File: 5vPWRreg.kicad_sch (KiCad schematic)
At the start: 25 parts, among them U9 TPS54561DPRR

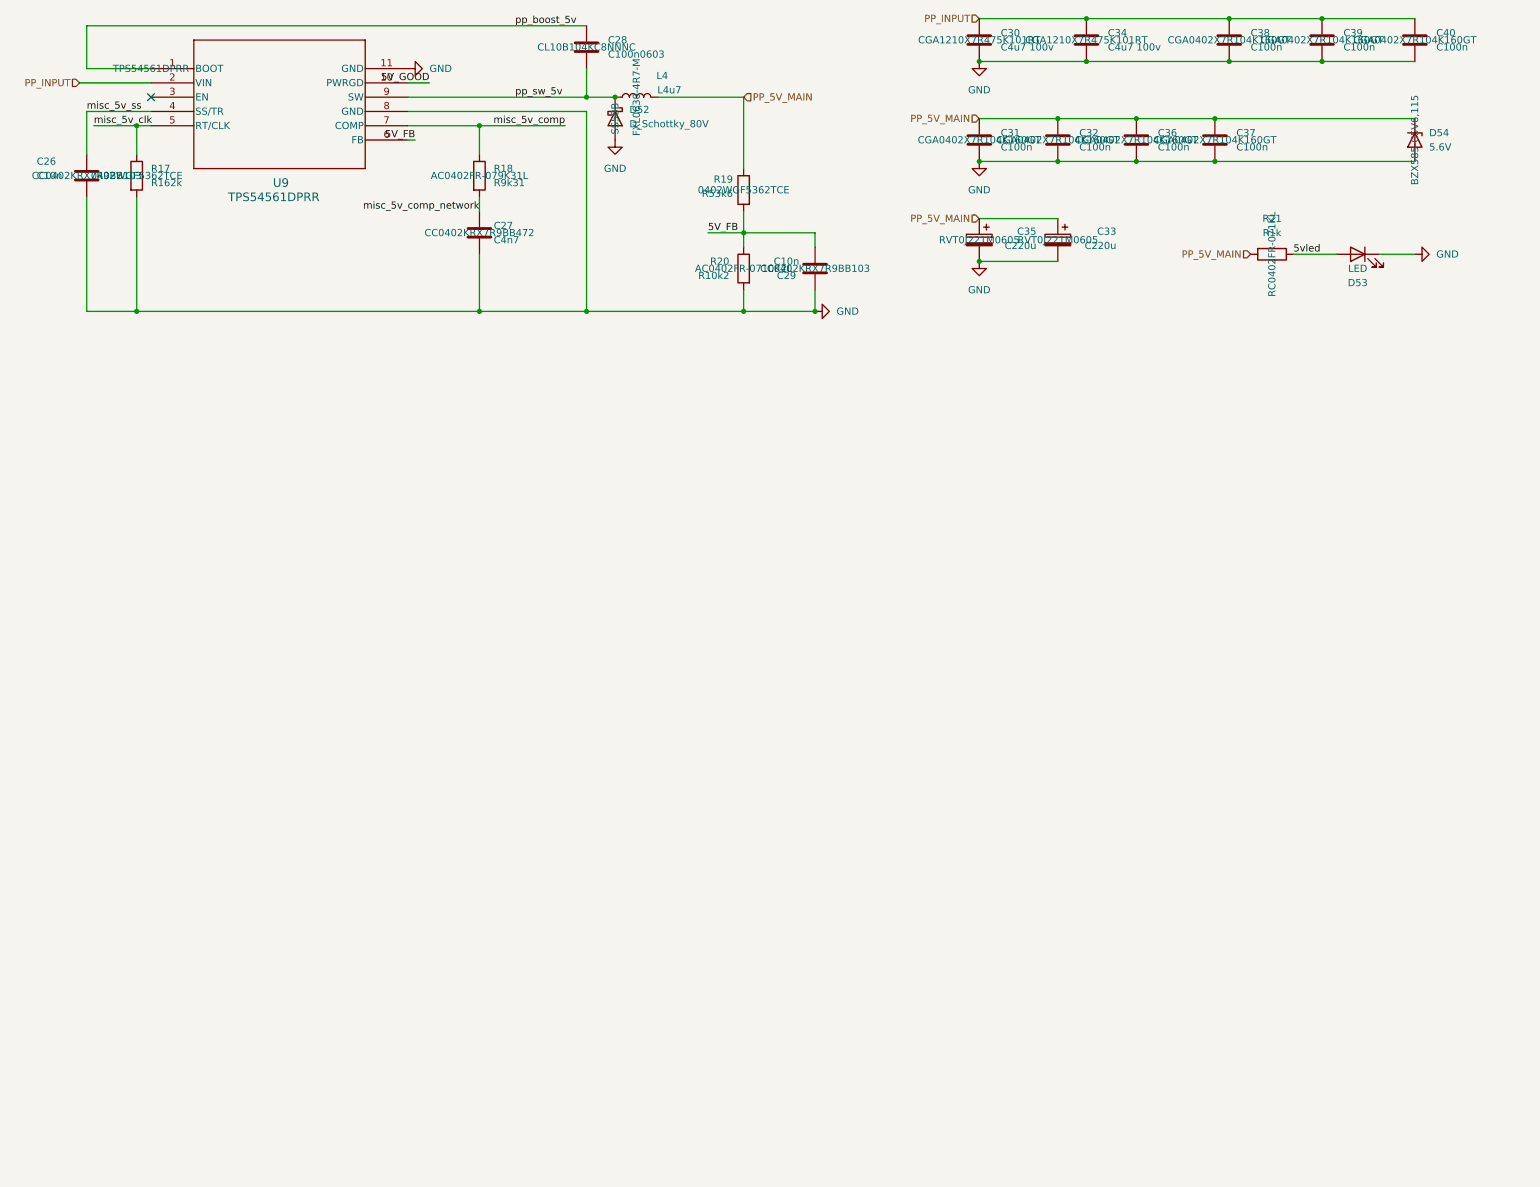
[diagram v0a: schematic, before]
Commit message: 5 volt regulator for PVT
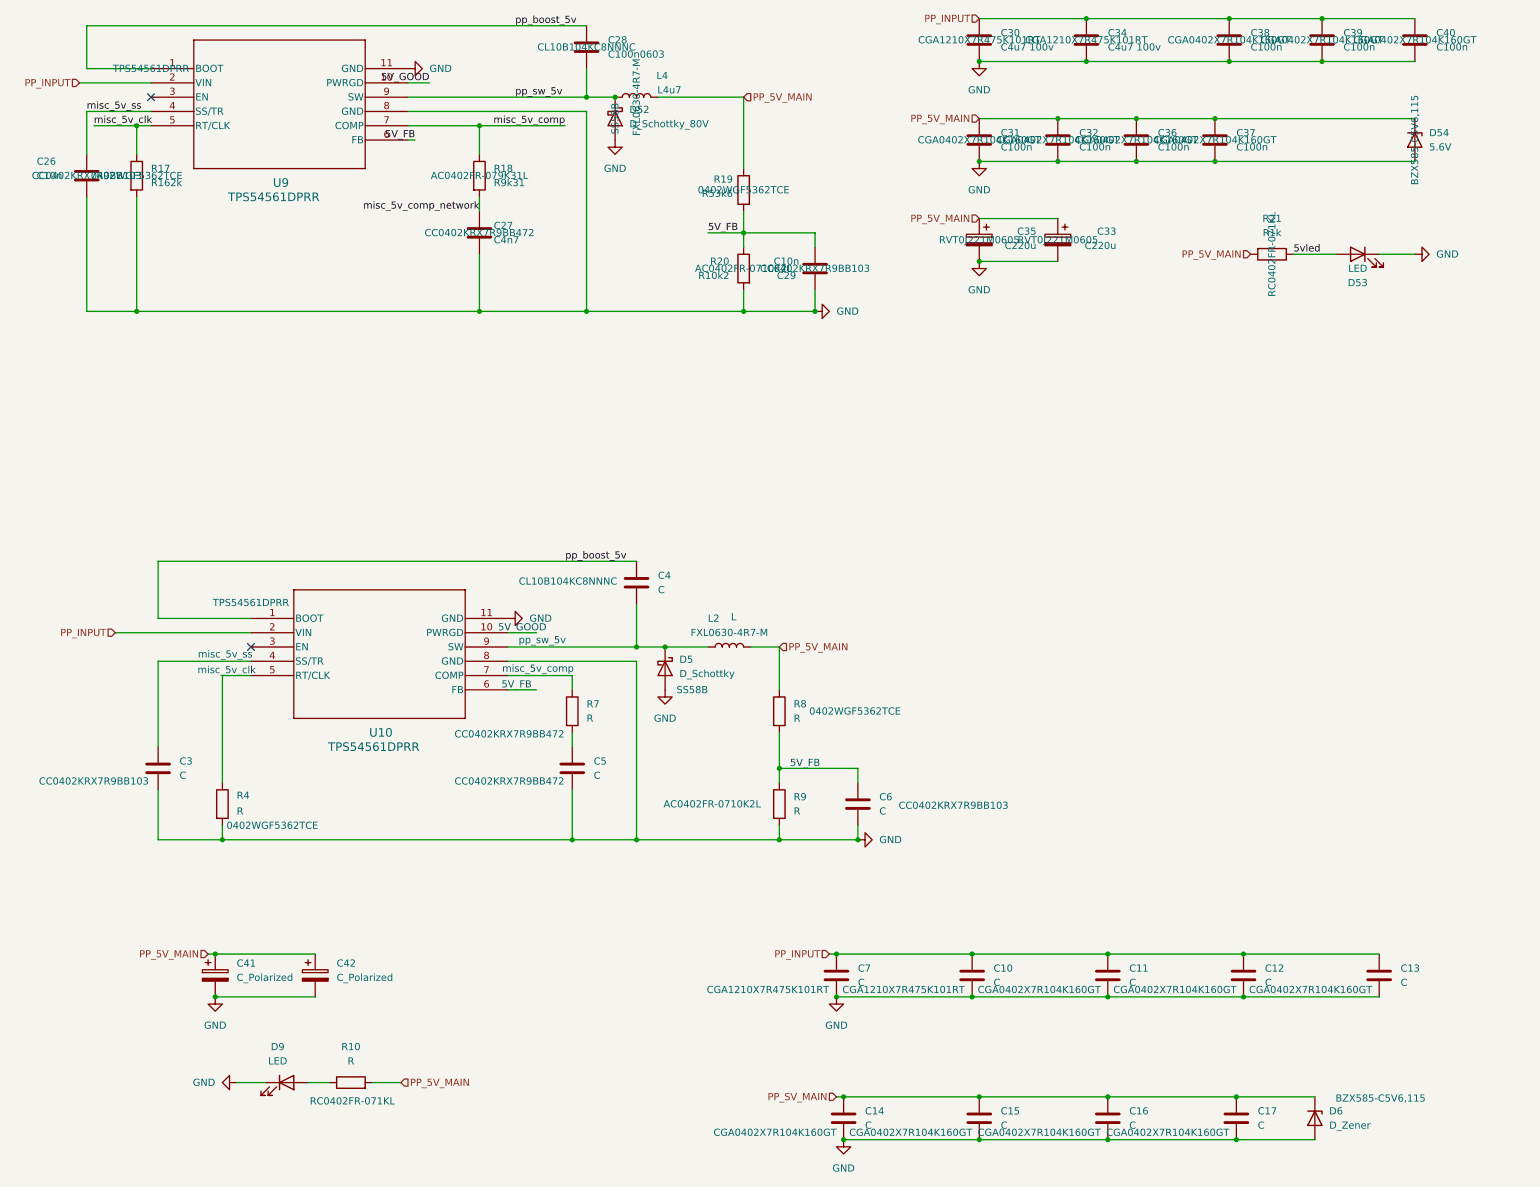
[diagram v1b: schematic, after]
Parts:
- added C10, C11, C12, C13, C14, C15, C16, C17, C3, C4, C5, C6, C7: C, symbol Device:C
- added C41, C42: C_Polarized, symbol Device:C_Polarized
- added D5: D_Schottky, symbol Device:D_Schottky
- added D6: D_Zener, symbol Device:D_Zener
- added D9: LED, symbol Device:LED
- added L2: L, symbol Device:L
- added R10, R4, R7, R8, R9: R, symbol Device:R
- added U10: TPS54561DPRR, WSON10_DPR_TEX, symbol jack_stand_board_symbols:TPS54561DPRR
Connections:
- net GND: now also C10.2, C11.2, C12.2, C13.2, C14.2, C15.2, C16.2, C17.2, C3.2, C41.2, C42.2, C5.2, C6.2, C7.2, D5.2 (A), D6.2 (A), D9.1 (K), R4.2, R9.2, U10.11 (GND), U10.8 (GND)
- net PP_5V_MAIN: now also C41.1, C42.1, L2.2, R10.2, R8.1
- net PP_INPUT: now also C10.1, C11.1, C12.1, C13.1, C7.1, U10.2 (VIN)
- net pp_boost_5v: now also C4.1, U10.1 (BOOT)
- new net: C3.1, U10.4 (SS/TR)
- new net: R4.1, U10.5 (RT/CLK)
- new net: R7.1, U10.7 (COMP)
- new net: C4.2, D5.1 (K), L2.1, U10.9 (SW)
- new net: C5.1, R7.2
- new net: D9.2 (A), R10.1
- new net: C6.1, R8.2, R9.1
- new net PP_SV_MAIN: C14.1, C15.1, C16.1, C17.1, D6.1 (K)
- no-connect marks 1 -> 2
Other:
- note added: "5V_FB"
- note added: "5V_GOOD"
- note added: "misc_5v_clk"
- note added: "misc_5v_comp"
- note added: "misc_5v_ss"
- note added: "pp_sw_5v"

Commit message: layout
Signed-off-by: sanyue <sanyue7th@gmail.com>
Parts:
- removed C10, C11, C12, C13, C14, C15, C16, C17, C3, C4, C5, C6, C7: C, symbol Device:C
- removed C41, C42: C_Polarized, symbol Device:C_Polarized
- removed D5: D_Schottky, symbol Device:D_Schottky
- removed D6: D_Zener, symbol Device:D_Zener
- removed D9: LED, symbol Device:LED
- removed L2: L, symbol Device:L
- removed R10, R4, R7, R8, R9: R, symbol Device:R
- removed U10: TPS54561DPRR, WSON10_DPR_TEX, symbol jack_stand_board_symbols:TPS54561DPRR
- U9: footprint WSON10_DPR_TEX -> aaafootprintlib:WSON10_DPR_TEX
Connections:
- no-connect marks 2 -> 1
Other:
- note removed: "5V_FB"
- note removed: "5V_GOOD"
- note removed: "misc_5v_clk"
- note removed: "misc_5v_comp"
- note removed: "misc_5v_ss"
- note removed: "pp_sw_5v"
- moved on the sheet: C26, C27, C28, C29, C30, C31, C32, C33, C34, C35, C36, C37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
